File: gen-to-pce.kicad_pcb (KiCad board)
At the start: 2 copper layers, 69.8 x 31.8 mm, 12 parts, among them J1 DB9 (M), J2 M-DIN-8 (F), SW1 SW_DPDT_x2, U1 74HC04, U2 74HC74, U3 74HC157

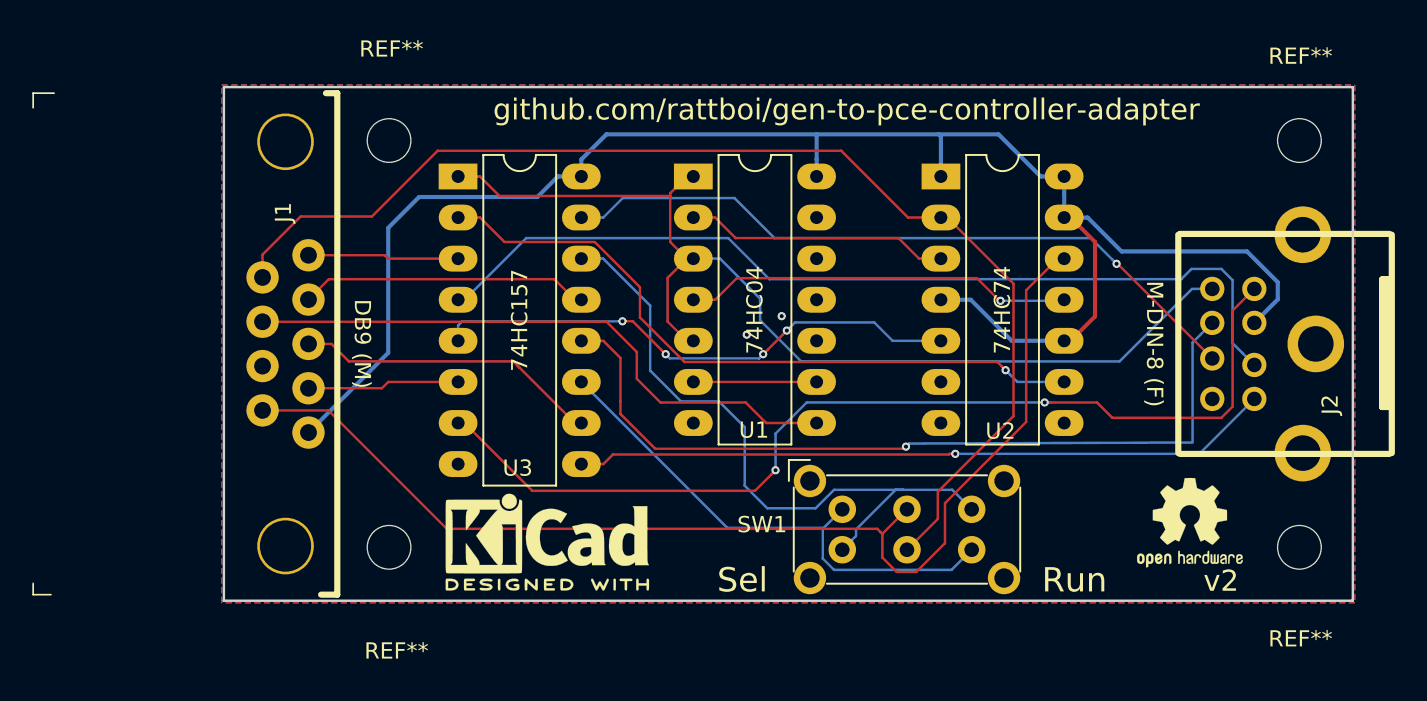
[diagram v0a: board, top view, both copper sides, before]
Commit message: Update to v2.1, wider +5V traces, added decoupling cap
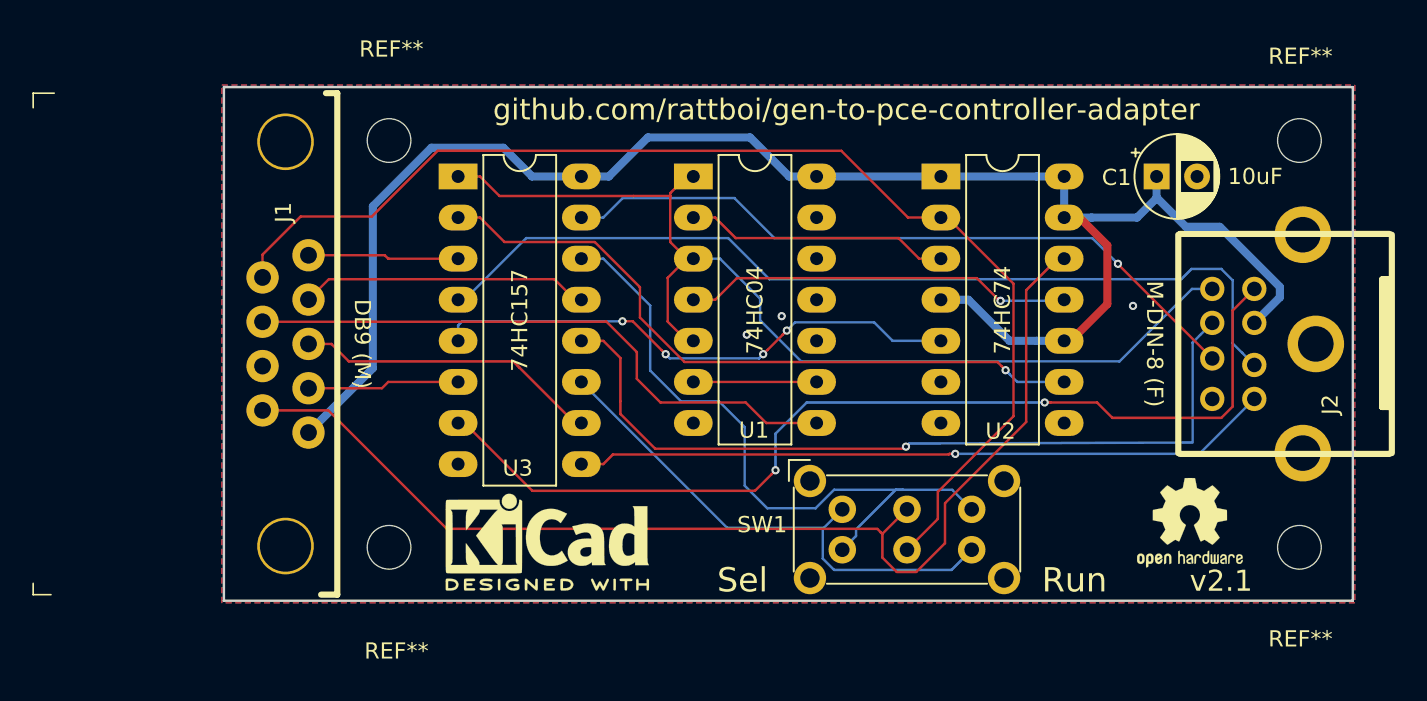
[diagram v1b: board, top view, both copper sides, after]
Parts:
- added C1: 10uF, Capacitor_THT:CP_Radial_D5.0mm_P2.50mm, F.Cu at (155.4, 77.3)
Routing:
- net GND: vias 2 -> 3
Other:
- board text added: "v2.1"
- board text removed: "v2"
